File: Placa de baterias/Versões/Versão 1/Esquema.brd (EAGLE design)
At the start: 35.5 x 12.6 mm, 3 parts

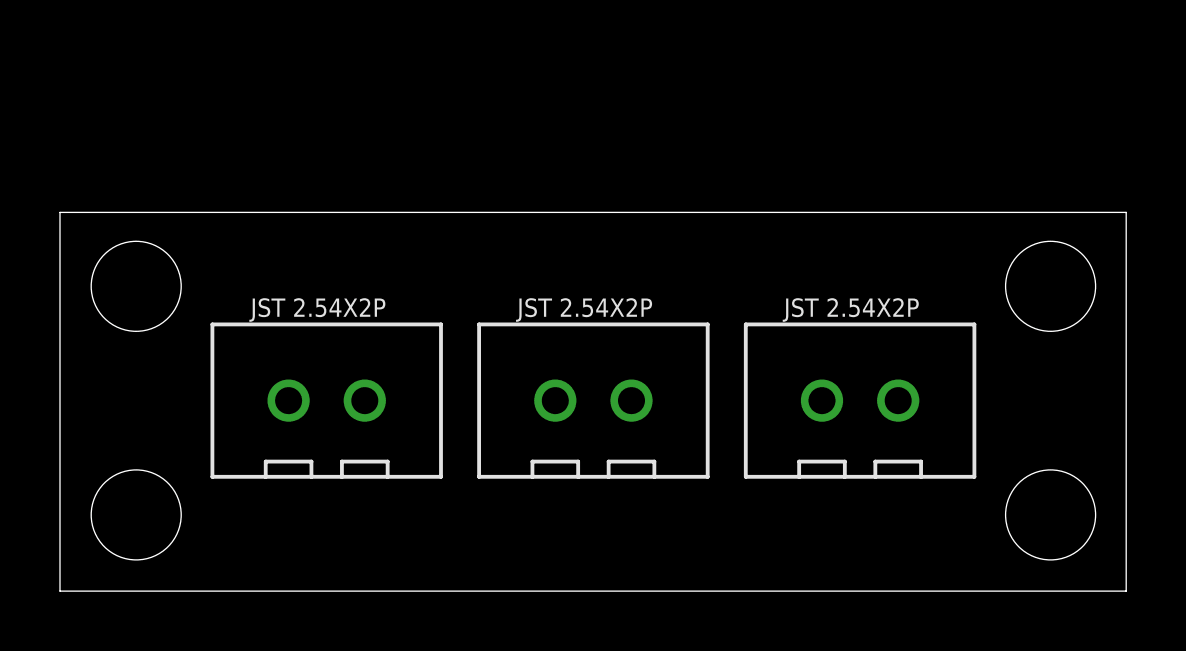
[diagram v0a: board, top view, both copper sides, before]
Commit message: mudanças na placa de processamento
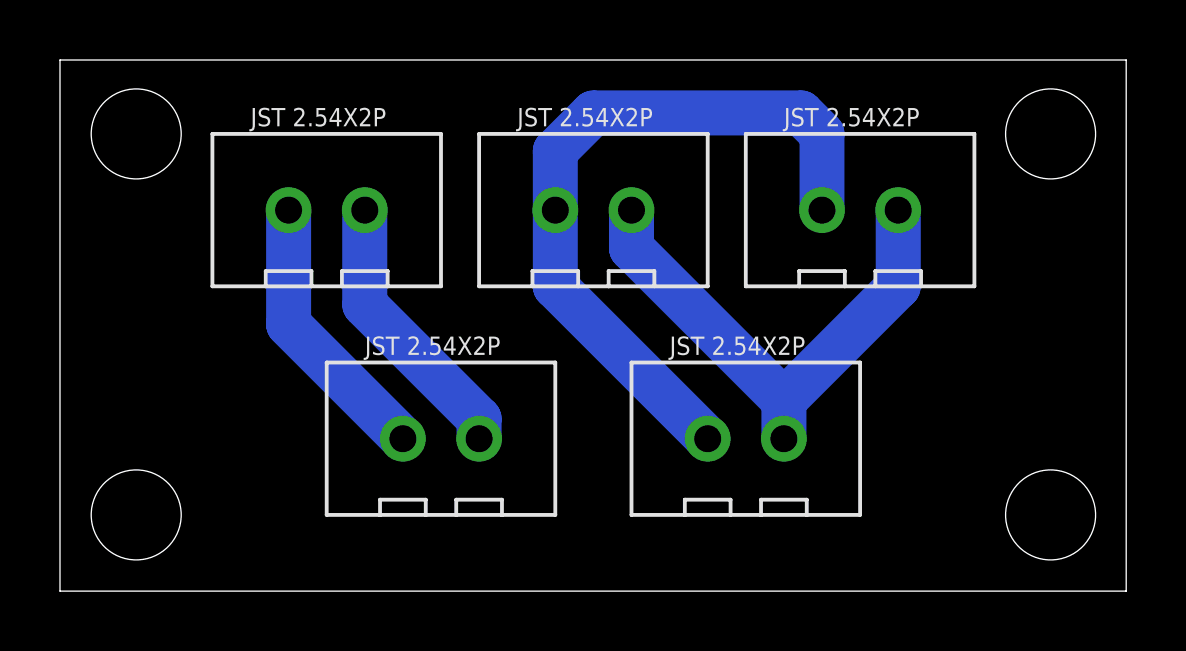
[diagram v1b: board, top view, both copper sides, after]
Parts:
- added U$4, U$5: JST2.54X2P, CRD:JST2.54X2P_FOOTPRINT
- moved U$1 10.9 mm to (8.89, 12.7)
- moved U$2 10.9 mm to (17.8, 12.7)
- moved U$3 6.35 mm to (26.7, 12.7)
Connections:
- new net V1+: U$1.1, U$4.1
- new net V1-: U$1.2, U$4.2
- new net V2+: U$2.1, U$3.1, U$5.1
- new net V2-: U$2.2, U$3.2, U$5.2
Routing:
- net V2+: track 0.00 -> 23.9 mm
- net V2-: track 0.00 -> 17.7 mm
- net V1-: track 0.00 -> 9.20 mm
- net V1+: track 0.00 -> 9.20 mm
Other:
- board size 35.5 x 12.6 mm -> 35.5 x 17.7 mm
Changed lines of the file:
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@@
 </layers>
 <board>
-<fusionsync huburn="a.YnVzaW5lc3M6ZGlzY2VudGUxNzg" projecturn="a.YnVzaW5lc3M6ZGlzY2VudGUxNzgjRDIwMjIwNjExNTMyNjQzNTAx" f3durn="urn:adsk.wipprod:dm.lineage:Dvtrc6K0SWqyUMVJzSpTWQ" pcbguid="4c150170-9bfb-4150-a035-c697c5894ec7" lastpulledtime="" lastsyncedchangeguid="" latestrevisionid="d102113a-d883-4e5e-9b53-b046faa94ace" lastsyncedrevisionid="d102113a-d883-4e5e-9b53-b046faa94ace" lastboardhashguid="886122b8-1ca9-acbc-cb29-0f94381838a5" lastpushedtime="2024-10-25T16:06:24Z" linktopcb3d="true"/>
+<fusionsync huburn="a.YnVzaW5lc3M6ZGlzY2VudGUxNzg" projecturn="a.YnVzaW5lc3M6ZGlzY2VudGUxNzgjRDIwMjIwNjExNTMyNjQzNTAx" f3durn="urn:adsk.wipprod:dm.lineage:Dvtrc6K0SWqyUMVJzSpTWQ" pcbguid="" lastpulledtime="" lastsyncedchangeguid="" latestrevisionid="d102113a-d883-4e5e-9b53-b046faa94ace" lastsyncedrevisionid="d102113a-d883-4e5e-9b53-b046faa94ace" lastboardhashguid="886122b8-1ca9-acbc-cb29-0f94381838a5" lastpushedtime="2024-10-25T16:06:24Z" linktopcb3d="true"/>
 <plain>
 <wire x1="0" y1="0" x2="35.54" y2="0" width="0" layer="20"/>
-<wire x1="35.54" y1="0" x2="35.54" y2="12.624" width="0" layer="20"/>
-<wire x1="35.54" y1="12.624" x2="0" y2="12.624" width="0" layer="20"/>
-<wire x1="0" y1="12.624" x2="0" y2="0" width="0" layer="20"/>
+<wire x1="35.54" y1="0" x2="35.54" y2="17.704" width="0" layer="20"/>
+<wire x1="35.54" y1="17.704" x2="0" y2="17.704" width="0" layer="20"/>
+<wire x1="0" y1="17.704" x2="0" y2="0" width="0" layer="20"/>
 <hole x="2.54" y="2.54" drill="3"/>
+<hole x="2.54" y="15.24" drill="3"/>
+<hole x="33.02" y="15.24" drill="3"/>
 <hole x="33.02" y="2.54" drill="3"/>
-<hole x="2.54" y="10.16" drill="3"/>
-<hole x="33.02" y="10.16" drill="3"/>
 </plain>
 <attributes>
@@
 <param name="mtCopper" value="0.035mm 0.035mm 0.035mm 0.035mm 0.035mm 0.035mm 0.035mm 0.035mm 0.035mm 0.035mm 0.035mm 0.035mm 0.035mm 0.035mm 0.035mm 0.035mm"/>
 <param name="mtIsolate" value="1.5mm 0.15mm 0.2mm 0.15mm 0.2mm 0.15mm 0.2mm 0.15mm 0.2mm 0.15mm 0.2mm 0.15mm 0.2mm 0.15mm 0.2mm"/>
-<param name="mdWireWire" value="6mil"/>
-<param name="mdWirePad" value="6mil"/>
-<param name="mdWireVia" value="6mil"/>
+<param name="mdWireWire" value="30mil"/>
+<param name="mdWirePad" value="20mil"/>
+<param name="mdWireVia" value="20mil"/>
 <param name="mdPadPad" value="6mil"/>
 <param name="mdPadVia" value="6mil"/>
@@
 <param name="mdDrill" value="6mil"/>
 <param name="mdSmdStop" value="0mil"/>
-<param name="msWidth" value="6mil"/>
-<param name="msDrill" value="0.35mm"/>
+<param name="msWidth" value="1.5mm"/>
+<param name="msDrill" value="1mm"/>
 <param name="msMicroVia" value="9.99mm"/>
 <param name="msBlindViaRatio" value="0.5"/>
-<param name="rvPadTop" value="0.25"/>
+<param name="rvPadTop" value="0.35"/>
 <param name="rvPadInner" value="0.25"/>
-<param name="rvPadBottom" value="0.25"/>
+<param name="rvPadBottom" value="0.35"/>
 <param name="rvViaOuter" value="0.25"/>
 <param name="rvViaInner" value="0.25"/>
@@
 <param name="rvMicroViaInner" value="0.25"/>
 <param name="rlMinPadTop" value="10mil"/>
-<param name="rlMaxPadTop" value="20mil"/>
+<param name="rlMaxPadTop" value="30mil"/>
 <param name="rlMinPadInner" value="10mil"/>
 <param name="rlMaxPadInner" value="20mil"/>
 <param name="rlMinPadBottom" value="10mil"/>
-<param name="rlMaxPadBottom" value="20mil"/>
+<param name="rlMaxPadBottom" value="30mil"/>
 <param name="rlMinViaOuter" value="8mil"/>
 <param name="rlMaxViaOuter" value="20mil"/>
@@
 </autorouter>
 <elements>
-<element name="U$1" library="CRD" library_urn="urn:adsk.eagle:library:39051337" package="JST2.54X2P_FOOTPRINT" package3d_urn="urn:adsk.eagle:package:39191967/2" value="JST2.54X2P" x="17.78" y="6.35" smashed="yes"/>
-<element name="U$2" library="CRD" library_urn="urn:adsk.eagle:library:39051337" package="JST2.54X2P_FOOTPRINT" package3d_urn="urn:adsk.eagle:package:39191967/2" value="JST2.54X2P" x="8.89" y="6.35" smashed="yes"/>
-<element name="U$3" library="CRD" library_urn="urn:adsk.eagle:library:39051337" package="JST2.54X2P_FOOTPRINT" package3d_urn="urn:adsk.eagle:package:39191967/2" value="JST2.54X2P" x="26.67" y="6.35" smashed="yes"/>
+<element name="U$1" library="CRD" library_urn="urn:adsk.eagle:library:39051337" package="JST2.54X2P_FOOTPRINT" package3d_urn="urn:adsk.eagle:package:39191967/2" value="JST2.54X2P" x="8.89" y="12.7" smashed="yes"/>
+<element name="U$2" library="CRD" library_urn="urn:adsk.eagle:library:39051337" package="JST2.54X2P_FOOTPRINT" package3d_urn="urn:adsk.eagle:package:39191967/2" value="JST2.54X2P" x="17.78" y="12.7" smashed="yes"/>
+<element name="U$3" library="CRD" library_urn="urn:adsk.eagle:library:39051337" package="JST2.54X2P_FOOTPRINT" package3d_urn="urn:adsk.eagle:package:39191967/2" value="JST2.54X2P" x="26.67" y="12.7" smashed="yes"/>
+<element name="U$4" library="CRD" library_urn="urn:adsk.eagle:library:39051337" package="JST2.54X2P_FOOTPRINT" package3d_urn="urn:adsk.eagle:package:39191967/2" value="JST2.54X2P" x="12.7" y="5.08" smashed="yes"/>
+<element name="U$5" library="CRD" library_urn="urn:adsk.eagle:library:39051337" package="JST2.54X2P_FOOTPRINT" package3d_urn="urn:adsk.eagle:package:39191967/2" value="JST2.54X2P" x="22.86" y="5.08" smashed="yes"/>
 </elements>
 <signals>
+<signal name="V1+">
+<contactref element="U$4" pad="1"/>
+<contactref element="U$1" pad="1"/>
+<wire x1="11.43" y1="5.08" x2="7.62" y2="8.89" width="1.5" layer="16"/>
+<wire x1="7.62" y1="8.89" x2="7.62" y2="12.7" width="1.5" layer="16"/>
+</signal>
+<signal name="V1-">
+<contactref element="U$4" pad="2"/>
+<contactref element="U$1" pad="2"/>
+<wire x1="13.97" y1="5.08" x2="13.97" y2="5.73895625" width="1.5" layer="16"/>
+<wire x1="13.97" y1="5.73895625" x2="10.16" y2="9.54895625" width="1.5" layer="16"/>
+<wire x1="10.16" y1="9.54895625" x2="10.16" y2="12.7" width="1.5" layer="16"/>
+</signal>
+<signal name="V2+">
+<contactref element="U$5" pad="1"/>
+<contactref element="U$2" pad="1"/>
+<contactref element="U$3" pad="1"/>
+<wire x1="16.51" y1="12.7" x2="16.51" y2="10.16" width="1.5" layer="16"/>
+<wire x1="16.51" y1="10.16" x2="21.59" y2="5.08" width="1.5" layer="16"/>
+<wire x1="16.51" y1="14.668" x2="17.78" y2="15.938" width="1.5" layer="16"/>
+<wire x1="17.78" y1="15.938" x2="24.702" y2="15.938" width="1.5" layer="16"/>
+<wire x1="24.702" y1="15.938" x2="25.4" y2="15.24" width="1.5" layer="16"/>
+<wire x1="25.4" y1="15.24" x2="25.4" y2="12.7" width="1.5" layer="16"/>
+<wire x1="16.51" y1="12.7" x2="16.51" y2="14.668" width="1.5" layer="16"/>
+</signal>
+<signal name="V2-">
+<contactref element="U$5" pad="2"/>
+<contactref element="U$2" pad="2"/>
+<contactref element="U$3" pad="2"/>
+<wire x1="19.05" y1="11.43" x2="19.05" y2="12.7" width="1.5" layer="16"/>
+<wire x1="24.13" y1="5.08" x2="24.13" y2="6.35" width="1.5" layer="16"/>
+<wire x1="24.13" y1="6.35" x2="19.05" y2="11.43" width="1.5" layer="16"/>
+<wire x1="24.13" y1="6.35" x2="27.94" y2="10.16" width="1.5" layer="16"/>
+<wire x1="27.94" y1="10.16" x2="27.94" y2="12.7" width="1.5" layer="16"/>
+</signal>
 </signals>
 <mfgpreviewcolors>
